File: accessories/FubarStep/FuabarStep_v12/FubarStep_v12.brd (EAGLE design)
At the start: 100.1 x 54.6 mm, 61 parts, among them IC2 SN754410NE, IC3 SN754410NE, U1 FUBARINO_SD, U2 FUBARINO_MINI, U3 OKI-78SR-5/1.5-W36H-C, X1 DC21MMX

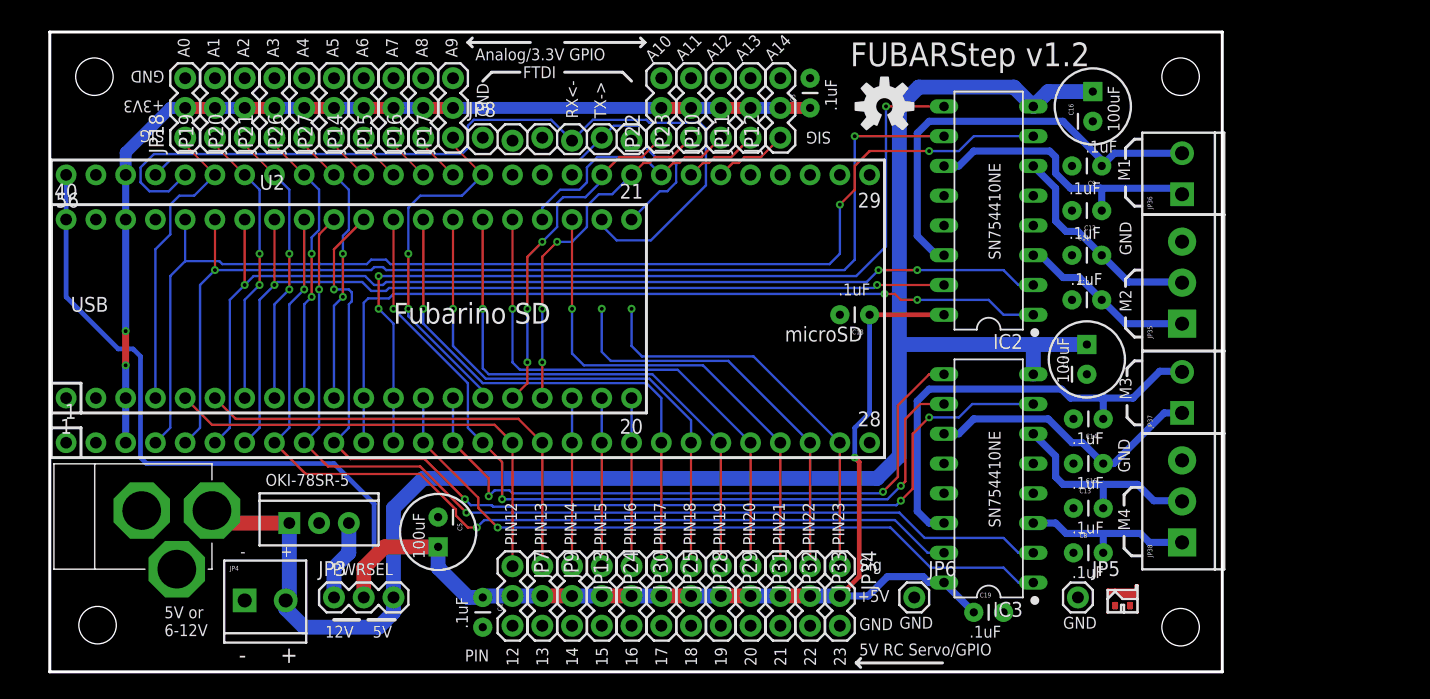
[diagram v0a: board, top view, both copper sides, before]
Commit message: Just playing with some ideas for v1.2 board - adding headers to every pin, for a complete break out board type feel.
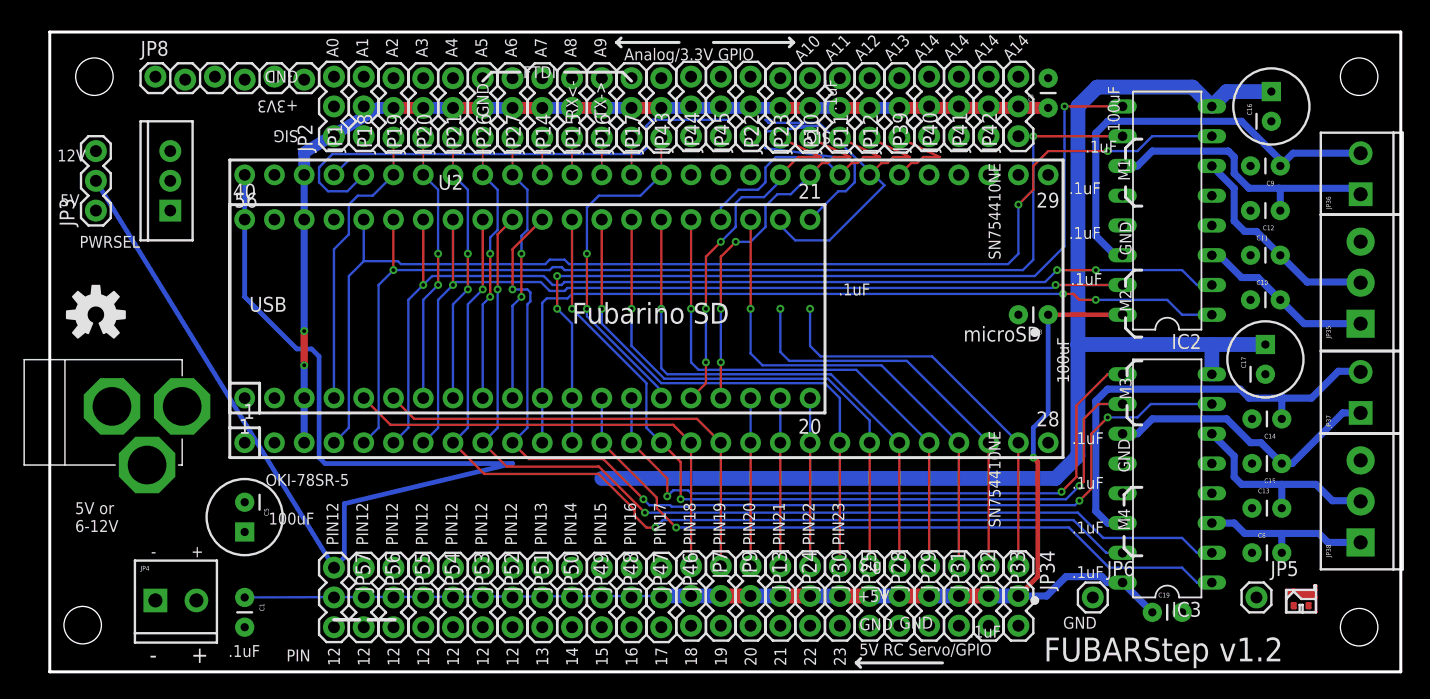
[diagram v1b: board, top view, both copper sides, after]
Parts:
- added JP1, JP2, JP39, JP40, JP41, JP42, JP43, JP44, JP45, JP46, JP47, JP48, JP49, JP50, JP51, JP52, JP53, JP54, JP55, JP56, JP57: (no value), SparkFun-Connectors:1X03
- moved LOGO1 69.6 mm to (3.81, 30.5)
- moved JP3 38.8 mm to (3.81, 39.4), turned to 90 degrees
- moved U3 31.9 mm to (10.2, 41.9), turned to 90 degrees
- moved JP8 28.4 mm to (8.89, 50.8)
- moved C3 20.3 mm to (85.1, 48.1)
- moved C1 20.3 mm to (16.5, 6.35)
- moved JP14 17.8 mm to (44.5, 45.6)
- moved JP15 17.8 mm to (47.0, 45.6)
- moved JP16 17.8 mm to (49.5, 45.6)
- moved JP17 17.8 mm to (52.1, 45.6)
- moved JP18 17.8 mm to (29.2, 45.6)
- moved JP19 17.8 mm to (31.8, 45.6)
- moved JP20 17.8 mm to (34.3, 45.6)
- moved JP21 17.8 mm to (36.8, 45.6)
- moved JP26 17.8 mm to (39.4, 45.6)
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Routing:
- net +5V: track 149.3 -> 214.7 mm
- net VIN: track 145.6 -> 108.2 mm
- net RX: track 75.5 -> 68.6 mm
- net N$2: track 6.88 -> 0.00 mm
- net TX: track 55.0 -> 59.6 mm
- net 3.3V: track 84.8 -> 89.3 mm
- net A10: track 29.7 -> 31.2 mm
- net A12: track 20.7 -> 22.2 mm
- net A14: track 6.40 -> 7.87 mm
- net A13: track 6.40 -> 7.87 mm
- net A11: track 30.0 -> 31.5 mm
- net A5: track 4.23 -> 3.18 mm
- net A8: track 4.23 -> 3.18 mm
- net A7: track 4.23 -> 3.18 mm
- net A6: track 4.23 -> 3.18 mm
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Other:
- board size 100.1 x 54.6 mm -> 115.3 x 54.6 mm

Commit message: New version of FubarStep - almost ready to go.
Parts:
- moved X1 7.62 mm to (4.83, 15.1)
- moved U3 5.68 mm to (7.62, 36.8), turned to 180 degrees
- moved LOGO1 5.16 mm to (7.87, 27.3)
- moved C5 4.58 mm to (19.1, 9.40)
- moved JP1 4.57 mm to (26.7, 41.1)
- moved JP2 4.57 mm to (24.1, 41.1)
- moved JP39 4.57 mm to (74.9, 41.1)
- moved JP40 4.57 mm to (77.5, 41.1)
- moved JP41 4.57 mm to (80.0, 41.1)
- moved JP42 4.57 mm to (82.5, 41.1)
- moved JP43 4.57 mm to (54.6, 41.1)
- moved JP44 4.57 mm to (57.1, 41.1)
- moved JP45 4.57 mm to (59.7, 41.1)
- moved JP10 4.45 mm to (67.3, 41.1)
- moved JP11 4.45 mm to (69.8, 41.1)
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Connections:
- removed net +3V3: U1.40
- new net PIN24: JP42.1, U1.30
- new net PIN25: JP41.1, U1.31
- new net PIN26: JP40.1, U1.32
- new net PIN27: JP39.1, U1.33
- net +5V: now also JP46.2, JP47.2, JP48.2, JP49.2, JP50.2, JP51.2, JP52.2, JP53.2, JP54.2, JP55.2, JP56.2, JP57.2
- net 3.3V: now also JP1.2, JP2.2, JP39.2, JP40.2, JP41.2, JP42.2, JP43.2, JP44.1, JP44.2, JP45.2, U1.40
- net GND: now also JP1.3, JP2.3, JP39.3, JP40.3, JP41.3, JP42.3, JP43.1, JP43.3, JP44.3, JP45.3, JP46.3, JP47.3, JP48.3, JP49.3, JP50.3, JP51.3, JP52.3, JP53.3, JP54.3, JP55.3, JP56.3, JP57.3
- net M1A1: now also JP55.1
- net M1A2: now also JP57.1
- net M1A3: now also JP56.1
- net M1A4: now also JP54.1
- net M1EN12: now also JP50.1
- net M1EN34: now also JP49.1
- net M2A1: now also JP52.1
- net M2A2: now also JP51.1
- net M2A3: now also JP46.1
- net M2A4: now also JP53.1
- net M2EN12: now also JP48.1
- net M2EN34: now also JP47.1
- net RESET: now also JP45.1
- net RX: now also JP1.1
- net TX: now also JP2.1
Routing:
- net VIN: track 108.2 -> 175.1 mm, vias 0 -> 3
- net +5V: track 214.7 -> 155.5 mm, vias 1 -> 2
- net PIN22: track 35.2 -> 7.11 mm, vias 1 -> 0
- net PIN23: track 34.9 -> 7.11 mm, vias 1 -> 0
- net RX: track 68.6 -> 58.5 mm, vias 0 -> 1
- net 3.3V: track 89.3 -> 98.9 mm, vias 2 -> 0
- net M1EN34: track 76.0 -> 85.3 mm
- net M1EN12: track 70.1 -> 78.1 mm
- net M1A1: track 89.1 -> 96.8 mm
- net M1A4: track 77.9 -> 85.6 mm
- net A12: track 22.2 -> 14.6 mm
- net M1A2: track 101.1 -> 108.7 mm
- net M1A3: track 93.5 -> 100.6 mm
- net M2EN34: track 56.6 -> 62.1 mm, vias 2 -> 1
- net M2A1: track 86.2 -> 91.5 mm
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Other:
- board size 115.3 x 54.6 mm -> 115.6 x 49.5 mm
- board text added: "0"
- board text added: "1"
- board text added: "10"
- board text added: "11"
- board text added: "2"
- board text added: "24"
- board text added: "25"
- board text added: "26"
- board text added: "27"
- board text added: "28"
- board text added: "29"
- board text added: "3"
- board text added: "3V3"
- board text added: "4"
- board text added: "5"
- board text added: "6"
- board text added: "6-12V"
- board text added: "7"
- board text added: "8"
- board text added: "9"
- board text added: "PIN0"
- board text added: "PIN1"
- board text added: "PIN10"
- board text added: "PIN11"
- board text added: "PIN2"
- board text added: "PIN3"
- board text added: "PIN4"
- board text added: "PIN5"
- board text added: "PIN6"
- board text added: "PIN7"
- board text added: "PIN8"
- board text added: "PIN9"
- board text added: "RST"
- board text removed: "12V"
- board text removed: "PIN"
- board text removed: "Sig"

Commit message: Sent these boards off to Seeed for production.
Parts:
- removed C16, C17, C5: 100uF, SparkFun-Capacitors:CPOL-RADIAL-100UF-25V
- added C2, C4, C6: 100uF, SchmalzHaus:CPOL-RADIAL-100UF
- moved U$1 100.1 mm to (9.27, 25.5)
- moved LOGO1 4.26 mm to (3.68, 26.5)
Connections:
- net +5V: now also C2.1; no longer C5.1
- net GND: now also C2.2, C4.2, C6.2; no longer C16.2, C17.2, C5.2
- net VIN: now also C4.1, C6.1; no longer C16.1, C17.1
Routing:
- net M2A3: track 76.6 -> 78.5 mm
- net M2A1: track 91.5 -> 92.2 mm
- net VIN: track 175.1 -> 175.8 mm
